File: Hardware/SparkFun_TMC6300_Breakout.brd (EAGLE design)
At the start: 15.2 x 20.3 mm, 60 parts, among them U2 TMC6300

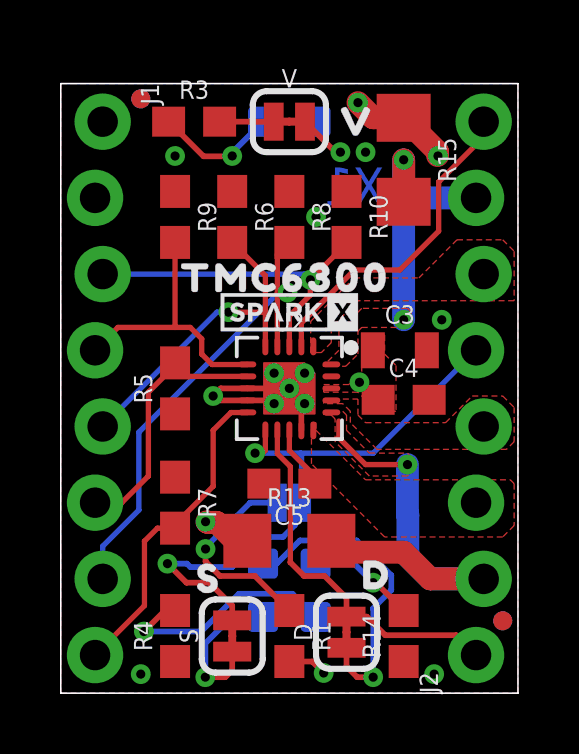
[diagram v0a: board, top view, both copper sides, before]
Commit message: Fix pinout to emulate other reprap style drivers
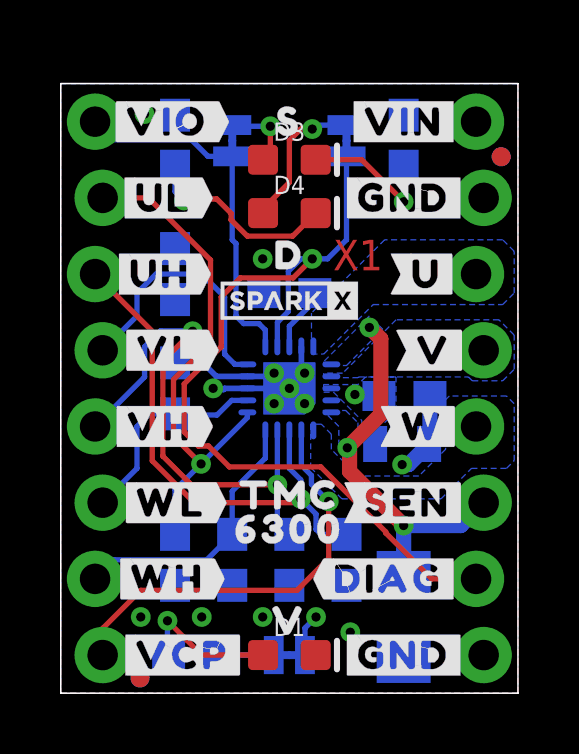
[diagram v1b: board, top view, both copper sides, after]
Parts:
- removed P: JUMPER-SMT_2_NO_SILK, SparkFun-Jumpers:SMT-JUMPER_2_NO_SILK
- removed R1: 100k, SparkFun-Resistors:0603
- removed R13: 0.12, SparkFun-Resistors:1206
- removed U$10: (no value), output:#U#4
- removed U$11: (no value), output:#V#5
- removed U$14: (no value), output:#W#3
- removed U$3: (no value), output:#UL#3
- removed U$5: (no value), output:#VH#6
- removed U$6: (no value), output:#VL#7
- removed U$7: (no value), output:#WH#4
- removed U$8: (no value), output:#WL#5
- added U$24: (no value), output:#VIN#0
- added U$28: (no value), output:#GND#1
- added U$30: (no value), output:#VH#2
- added U$31: (no value), output:#VL#3
- added U$32: (no value), output:#W#8
- added U$33: (no value), output:#WH#1
- added U$34: (no value), output:#WL#0
- U$2: device output:#UH#2 -> output:#SEN#0
- U$21: device output:P0 -> output:#UH#5
- U$22: device output:#RW#0 -> output:#UL#4
- U$25: device output:#RUV#0 -> output:#V#7
- U$4: device output:#VCC#0 -> output:#DIAG#0
- U$9: device output:#DIAG#2 -> output:#U#6
- moved FRAME1 38.1 mm to (26.7, -11.4), flipped to the bottom
- moved LOGO2 22.9 mm to (-3.81, 50.8), flipped to the bottom
- moved FD2 19.3 mm to (2.64, 0.51), flipped to the bottom, turned to 180 degrees
- moved FD3 19.3 mm to (2.64, 0.51), flipped to the top, turned to 180 degrees
- moved U$12 19.2 mm to (4.06, 1.27), flipped to the top
- moved R14 18.2 mm to (3.81, 18.4), flipped to the bottom, turned to 270 degrees
- moved R4 18.2 mm to (11.4, 18.4), flipped to the bottom, turned to 270 degrees
- moved U$26 17.8 mm to (9.53, 1.27), flipped to the bottom
- moved D1 17.8 mm to (7.62, 1.27), flipped to the top, turned to 0 degrees
- moved J1 17.8 mm to (1.27, 1.27), flipped to the bottom, turned to 90 degrees
- moved J2 17.8 mm to (14.0, 19.1), flipped to the bottom, turned to 270 degrees
- moved R3 17.8 mm to (4.45, 1.27), flipped to the bottom, turned to 180 degrees
- moved V 17.8 mm to (7.62, 1.27), flipped to the bottom, turned to 180 degrees
- moved U$4 16.8 mm to (10.9, 3.81), flipped to the top
- moved U$19 16.7 mm to (7.62, 19.1), flipped to the top
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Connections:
- removed net BRUV: J2.2, R13.2, U2.16
- removed net BRW: J2.7, R15.2, U2.20
- removed net N$2: P.2, R1.1
- removed net VCC: C3.1, C4.1, J1.1, R1.2, U2.18, V.2
- new net SENSE: J2.6, R15.2, U2.16, U2.20
- new net VIN: C3.1, C4.1, J2.1, U2.18, V.2
- net DIAG: now also J2.7; no longer J2.1
- net GND: now also J2.2, J2.8; no longer J1.2, R13.1
- net UH: now also J1.6; no longer J1.3
- net UL: now also J1.7; no longer J1.4
- net VCP: now also J1.1; no longer J2.8
- net VH: now also J1.4; no longer J1.7
- net VIO/!STDBY!: now also J1.8; no longer J2.5, P.1
- net VL: now also J1.5; no longer J1.8
- net W: now also J2.5; no longer J2.6
- net WH: now also J1.2; no longer J1.5
- net WL: now also J1.3; no longer J1.6
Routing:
- net DIAG: track 12.4 -> 28.2 mm, vias 0 -> 1
- net BRUV: track 14.7 -> 0.00 mm, vias 1 -> 0
- net SENSE: track 0.00 -> 12.6 mm, vias 0 -> 3
- net BRW: track 9.15 -> 0.00 mm, vias 2 -> 0
- net VIO/!STDBY!: track 20.8 -> 12.2 mm, vias 2 -> 0
- net UL: track 9.04 -> 17.2 mm, vias 0 -> 1
- net N$2: track 6.95 -> 0.00 mm, vias 1 -> 0
- net UH: track 11.3 -> 17.3 mm
- net N$9: track 10.4 -> 4.90 mm
- net GND: track 11.9 -> 8.12 mm, vias 15 -> 13
- net N$10: track 7.90 -> 4.69 mm
- net VCP: track 10.9 -> 14.0 mm, vias 0 -> 1
- net N$12: track 3.58 -> 6.63 mm
- net VCC: track 2.91 -> 0.00 mm, vias 3 -> 0
- net N$5: track 5.03 -> 2.50 mm
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- added copper zone on layer 16, net SENSE
- added copper zone on layer 16, net U
- added copper zone on layer 16, net V
- added copper zone on layer 15, net VIN
- added copper zone on layer 16, net VIN
- added copper zone on layer 16, net W
- removed copper zone on layer 1, net BRUV
- removed copper zone on layer 1, net BRW
- removed copper zone on layer 1, net U
- removed copper zone on layer 1, net V
- removed copper zone on layer 1, net VCC
- removed copper zone on layer 15, net VCC
- removed copper zone on layer 1, net W

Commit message: Fix DIAG label direction
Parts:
- renumbered U$4 to U$3
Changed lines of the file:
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@@
 <element name="U$24" library="output" package="#VIN#0" value="" x="11.43" y="19.05" smashed="yes"/>
 <element name="U$28" library="output" package="#GND#1" value="" x="11.43" y="1.27" smashed="yes"/>
-<element name="U$4" library="output" package="#DIAG#0" value="" x="10.922" y="3.81" smashed="yes"/>
 <element name="U$9" library="output" package="#U#6" value="" x="12.192" y="13.97" smashed="yes"/>
 <element name="U$21" library="output" package="#UH#5" value="" x="3.302" y="13.97" smashed="yes"/>
@@
 <element name="U$34" library="output" package="#WL#0" value="" x="3.683" y="6.35" smashed="yes"/>
 <element name="U$2" library="output" package="#SEN#0" value="" x="11.557" y="6.35" smashed="yes"/>
+<element name="U$3" library="output" package="#DIAG#0" value="" x="10.922" y="3.81" smashed="yes"/>
 </elements>
 <signals>
